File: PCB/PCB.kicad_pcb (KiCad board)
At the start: 2 copper layers, 88 x 50 mm, 52 parts, among them U1 STM32L010F4Px, U4 OPA344NA

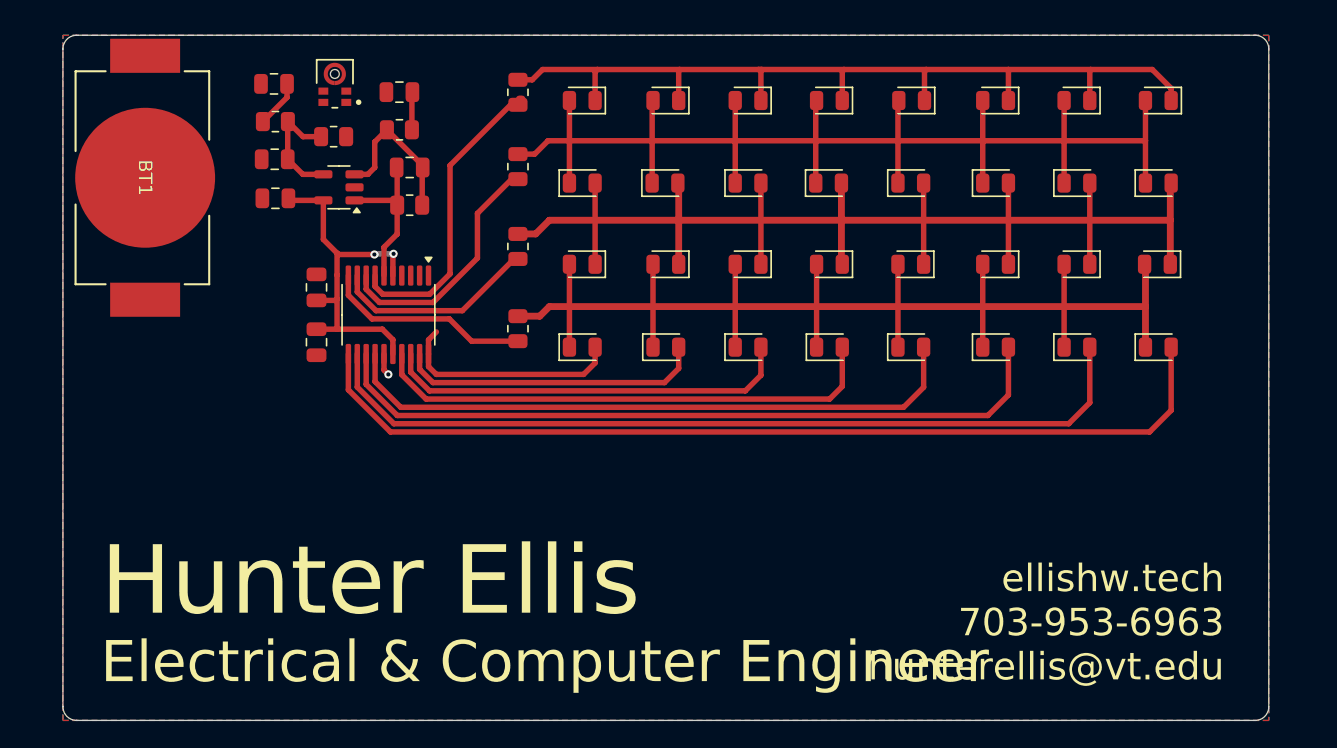
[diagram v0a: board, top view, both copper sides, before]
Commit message: MEMS microphone, SWD, and PCB trace USB power
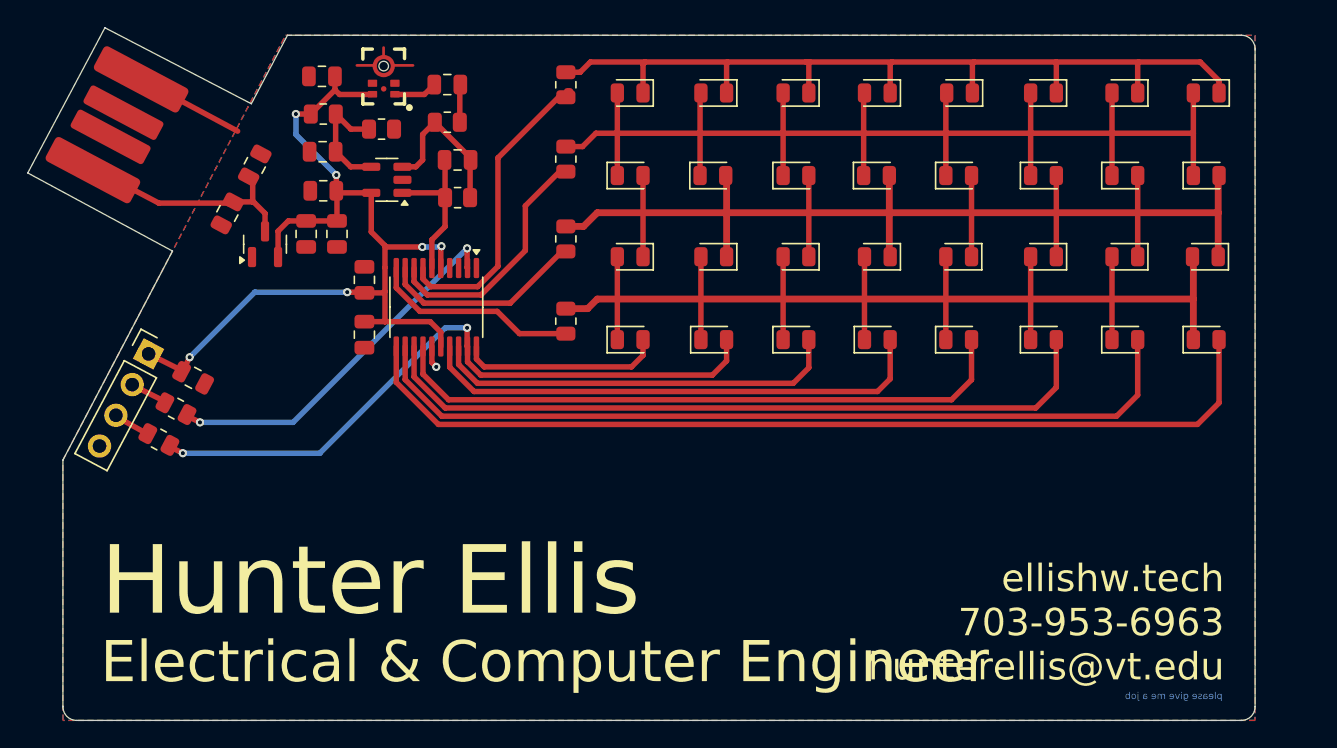
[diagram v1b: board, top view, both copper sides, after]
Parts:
- removed BT1: Battery_Cell, 1_Custom_Parts:BAT-HLD-012-SMT_TEC
- removed G***: LOGO, LOGO
- removed MK1: ~, 1_Custom_Parts:ICS-40180
- added C1: 100n, Capacitor_SMD:C_0805_2012Metric, F.Cu at (109.5, 125.0)
- added C10: 100n, Capacitor_SMD:C_0805_2012Metric, F.Cu at (114.0, 109.5)
- added C11: 10u, Capacitor_SMD:C_0805_2012Metric, F.Cu at (112.0, 113.0)
- added C12: 100n, Capacitor_SMD:C_0805_2012Metric, F.Cu at (117.8, 114.5)
- added C2: 10u, Capacitor_SMD:C_0805_2012Metric, F.Cu at (120.0, 114.5)
- added J1: Conn_01x04, Connector_PinHeader_2.54mm:PinHeader_1x04_P2.54mm_Vertical, F.Cu at (106.2, 123.2)
- added R10: 22, Resistor_SMD:R_0805_2012Metric, F.Cu at (107.0, 129.5)
- added R9: 22, Resistor_SMD:R_0805_2012Metric, F.Cu at (108.2, 127.2)
- added U2: ~, 1_Custom_Parts:PCB_USB, F.Cu at (103.9, 106.5)
- added U3: MCP1700-3302E_SOT23, Package_TO_SOT_SMD:SOT-23, F.Cu at (114.8, 115.2)
- added U5: ~, 1_Custom_Parts:SPH8878LR5H-1, F.Cu at (123.4, 102.3)
- moved D10 3.54 mm to (147.5, 116.2)
- moved D11 3.54 mm to (153.5, 116.2)
- moved D12 3.54 mm to (159.4, 116.2)
- moved D13 3.54 mm to (165.4, 116.2)
- moved D14 3.54 mm to (171.6, 116.2)
- moved D15 3.54 mm to (177.5, 116.2)
- moved D16 3.54 mm to (183.4, 116.2)
- moved D9 3.54 mm to (141.4, 116.2)
- moved R3 3.54 mm to (136.7, 109.0)
- moved C5 3.54 mm to (118.9, 103.0)
- moved C8 3.54 mm to (119.0, 108.5)
- moved D1 3.54 mm to (141.4, 122.2)
- moved D17 3.54 mm to (141.4, 110.2)
- moved D18 3.54 mm to (147.4, 110.2)
- moved D19 3.54 mm to (153.5, 110.2)
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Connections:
- net Net-(D2-A) renamed SWDIO
- U1 pad 2: unconnected-(U1-PC14-Pad2) -> SWCLK
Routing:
- net VCC: track 30.3 -> 64.9 mm, vias 2 -> 6
- net SWCLK: track 0.00 -> 26.2 mm, vias 0 -> 2
- net SWDIO: track 22.4 -> 48.3 mm, vias 0 -> 2
- net +5V: track 0.00 -> 11.9 mm
- net Net-(U5-OUT+): track 0.00 -> 3.23 mm
- net Net-(D1-A): track 16.7 -> 14.8 mm
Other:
- board size 88 x 50 mm -> 89.6 x 50.5 mm
- board text added: "please give me a job"
